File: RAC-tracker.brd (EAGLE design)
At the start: 31.8 x 97.8 mm, 37 parts, among them J1 U.FL, J2 U.FL, J5 U.FL, J6 U.FL, U2 SIM-ST-MFF2, U3 MCP73831, U4 NRF9160-SICA-R

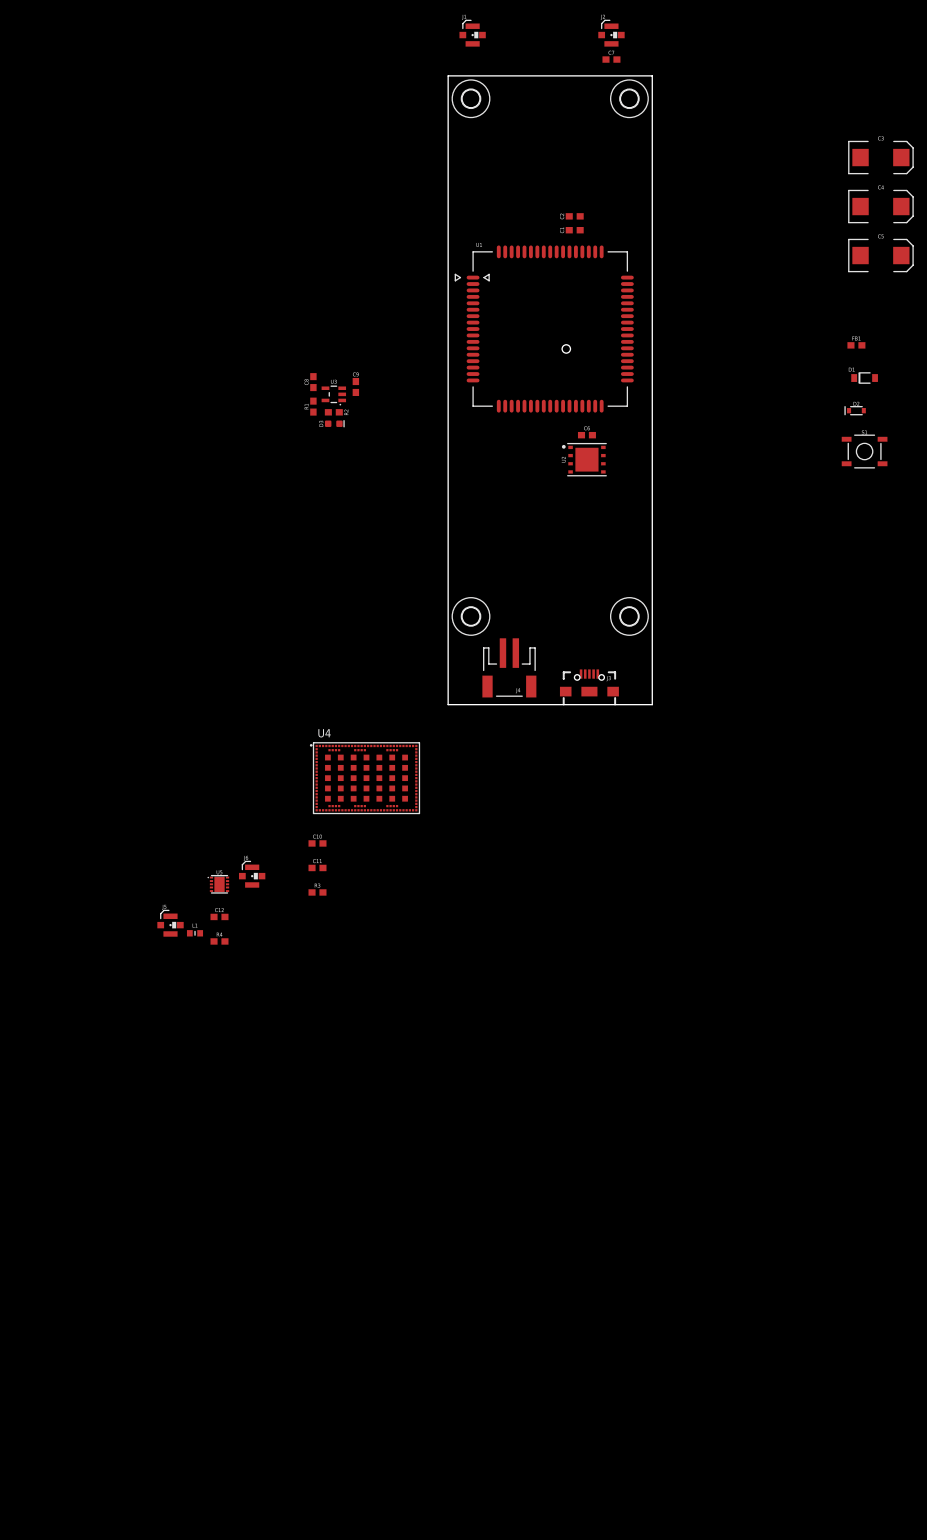
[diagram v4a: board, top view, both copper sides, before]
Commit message: Replaced GPS front-end, added 1.8V LDO
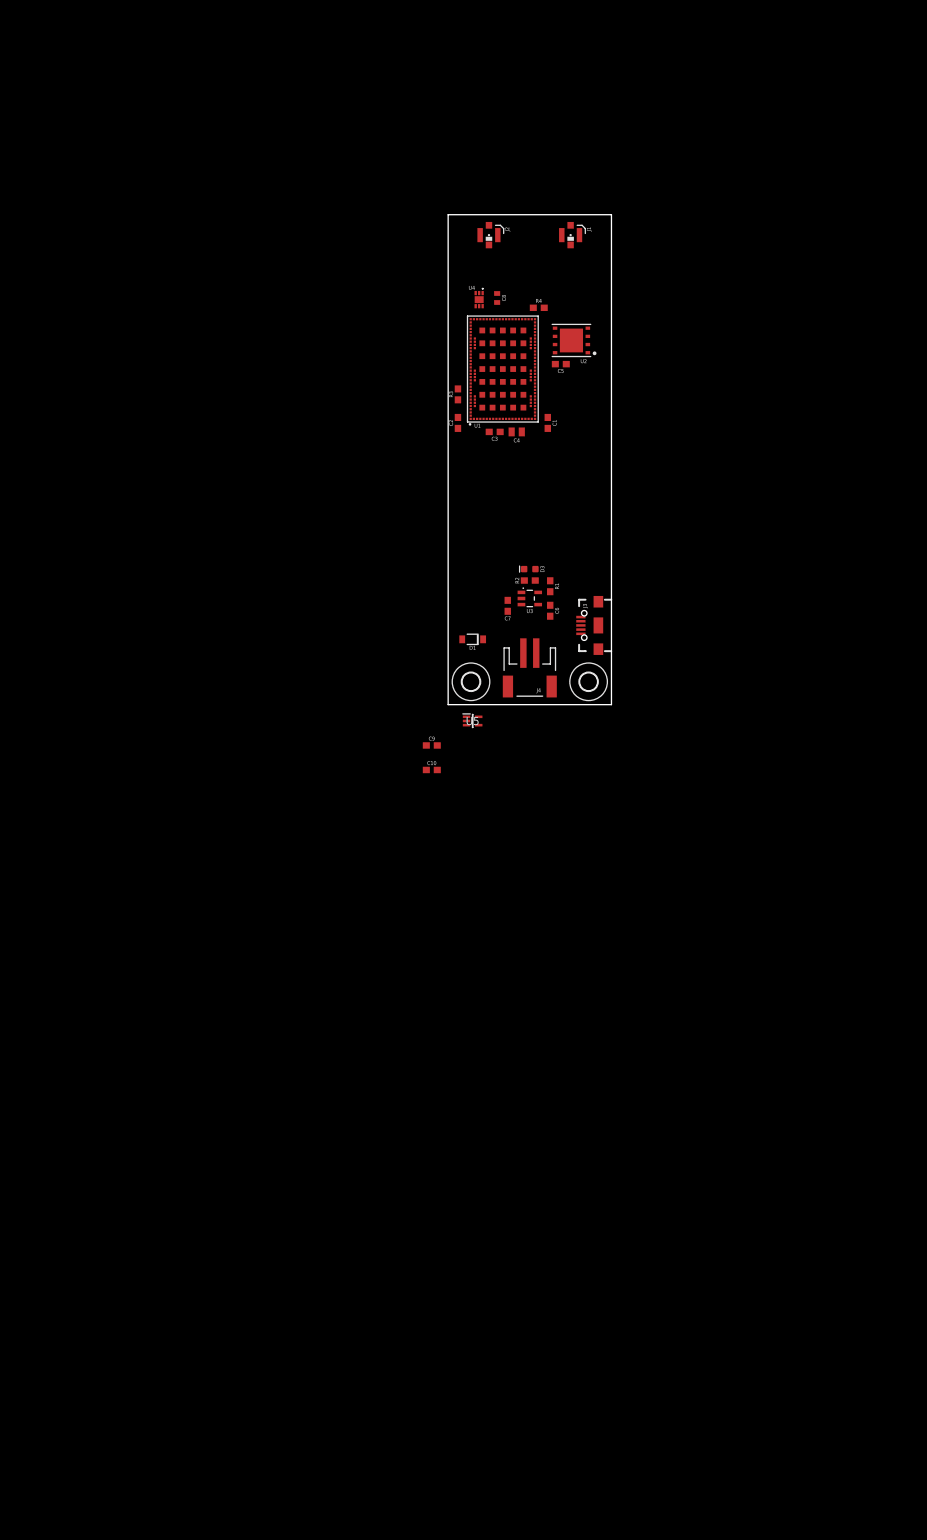
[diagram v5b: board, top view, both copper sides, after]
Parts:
- removed C11: 4.7uF, SparkFun-Capacitors:0603
- removed C12: 1nF, SparkFun-Capacitors:0603
- removed D2: 250mA/100V, SparkFun-DiscreteSemi:SOD-323
- removed FB1: 30Ω/1.8A, SparkFun-Coils:0603
- removed H3, H4: MOUNT-HOLE2.8, holes:2,8
- removed J5, J6: U.FL, SparkFun-Connectors:U.FL
- removed L1: 10nH, rocket-components:INDC1608X100N
- removed S1: MOMENTARY-SWITCH-SPST-SMD-5.2MM, SparkFun-Switches:TACTILE_SWITCH_SMD_5.2MM
- C1, C6: value 0.1uF -> 4.7uF
- C10, C9: value 4.7uF -> 1.0uF
- C2: value 1.0uF -> 4.7uF
- C3: value 100uF -> 4.7uF; device SparkFun-Capacitors:EIA7343 -> SparkFun-Capacitors:0603
- C4: value 100uF -> 47uF; device SparkFun-Capacitors:EIA7343 -> rocket-components:CAPC2012X145N
- C5: value 100uF -> 0.1uF; device SparkFun-Capacitors:EIA7343 -> SparkFun-Capacitors:0603
- C7: value 33pF -> 4.7uF
- C8: value 4.7uF -> 56pF; device SparkFun-Capacitors:0603 -> rocket-components:CAPC1608X90N
- U1: value (none) -> NRF9160-SICA-R; device rocket-components:SIM7000 -> rocket-components:NORDIC_NRF9160-SICA-R
- U4: value NRF9160-SICA-R -> SKY65723-81; device rocket-components:NORDIC_NRF9160-SICA-R -> rocket-components:SKY6572381
- U5: value (none) -> MIC5365-1.8YC5-TR; device rocket-components:HFFP10-CD -> rocket-components:SOT65P210X110-5N
- moved R4 110.4 mm to (14.1, 61.7), turned to 180 degrees
- moved H2 90.9 mm to (21.8, 3.56)
- moved H1 90.7 mm to (3.56, 3.56)
- moved C7 86.5 mm to (9.27, 15.4), turned to 90 degrees
- moved R3 80.5 mm to (1.52, 48.3), turned to 90 degrees
- moved U4 76.5 mm to (4.83, 63.0), turned to 180 degrees
- moved C3 73.7 mm to (7.24, 42.4), turned to 180 degrees
- moved D1 73.3 mm to (3.81, 10.2), turned to 180 degrees
- moved C4 66.6 mm to (10.7, 42.4)
- moved C9 57.0 mm to (-2.54, -6.35), turned to 0 degrees
- moved C5 52.6 mm to (17.5, 53.0)
- moved U5 46.9 mm to (3.81, -2.54)
- moved R1 46.2 mm to (15.9, 18.4), turned to 270 degrees
- moved U3 44.0 mm to (12.7, 16.5), turned to 270 degrees
- moved R2 40.2 mm to (12.7, 19.3), turned to 0 degrees
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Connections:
- removed net 3.3V: C11.1, C12.1, U4.12, U5.3
- removed net GNSS_OUT: C7.2, J2.FEED
- removed net GNSS_RF: C7.1, U1.53
- removed net IO_SUPPLY: U4.13
- removed net LTE_OUT: J1.FEED, U1.60
- removed net N$1: R3.1, U4.101
- removed net N$2: J6.FEED, U4.61
- removed net N$3: L1.2, U5.7
- removed net N$4: L1.1, U5.8
- removed net PWRKEY: D2.C, S1.3
- removed net PWRKEY_AN: D2.A, U1.1
- removed net RI: U1.4
- removed net RXD: U1.10
- removed net TXD: U1.9
- removed net VIN: C1.1, C2.1, C3.A, C4.A, C5.A, FB1.2, U1.55, U1.56, U1.57
- new net 1.8V: C10.1, C3.1, C8.1, U1.12, U4.1, U5.5
- new net EN: R3.1, U1.101
- new net IO_SUP: C4.1, U1.13
- new net LTE_ANT: J1.FEED, U1.61
- net GND: now also C3.2, C4.2, C5.2, C7.2, U1.1, U1.103_1, U1.103_10, U1.103_11, U1.103_12, U1.103_13, U1.103_14, U1.103_15, U1.103_16, U1.103_17, U1.103_18, U1.103_19, U1.103_2, U1.103_20, U1.103_21, U1.103_22, U1.103_23, U1.103_24, U1.103_25, U1.103_26, U1.103_27, U1.103_28, U1.103_29, U1.103_3, U1.103_30, U1.103_31, U1.103_32, U1.103_33, U1.103_34, U1.103_35, U1.103_4, U1.103_5, U1.103_6, U1.103_7, U1.103_8, U1.103_9, U1.14, U1.21, U1.27, U1.31, U1.36, U1.41, U1.44, U1.47, U1.5, U1.50, U1.52, U1.56, U1.60, U1.66, U1.72, U1.74, U1.75, U1.76, U1.77, U1.78, U1.79, U1.80, U1.81, U1.82, U1.85, U1.9, U1.90, U1.94, U1.98, U4.7; no longer C11.2, C12.2, C3.C, C4.C, C5.C, J5.1, J5.2, J6.1, J6.2, S1.1, U1.18, U1.2, U1.29, U1.39, U1.45, U1.46, U1.54, U1.58, U1.59, U1.61, U1.64, U4.1, U4.103_1, U4.103_10, U4.103_11, U4.103_12, U4.103_13, U4.103_14, U4.103_15, U4.103_16, U4.103_17, U4.103_18, U4.103_19, U4.103_2, U4.103_20, U4.103_21, U4.103_22, U4.103_23, U4.103_24, U4.103_25, U4.103_26, U4.103_27, U4.103_28, U4.103_29, U4.103_3, U4.103_30, U4.103_31, U4.103_32, U4.103_33, U4.103_34, U4.103_35, U4.103_4, U4.103_5, U4.103_6, U4.103_7, U4.103_8, U4.103_9, U4.14, U4.17, U4.21, U4.27, U4.31, U4.36, U4.41, U4.44, U4.47, U4.5, U4.50, U4.52, U4.56, U4.60, U4.62, U4.63, U4.65, U4.66, U4.72, U4.74, U4.75, U4.76, U4.77, U4.78, U4.79, U4.80, U4.81, U4.82, U4.85, U4.9, U4.90, U4.94, U4.98, U5.1, U5.4, U5.6, U5.9, U5.EP
- net GPS_ANT: now also J2.FEED, U4.3; no longer J5.FEED, U5.5
- net GPS_EN: now also U1.55, U4.2; no longer U4.55, U5.2
- net GPS_RF: now also U1.67, U4.6; no longer U4.67, U5.10
- net SIM_CLK: now also U1.46; no longer U1.32, U4.46
- net SIM_DATA: now also U1.48; no longer U1.31, U4.48
- net SIM_RST: now also U1.43; no longer U1.33, U4.43
- net SIM_VIN: now also C5.1, U1.49; no longer C6.1, U1.30, U4.49
- net USB_DM: no longer U1.28
- net USB_DP: no longer U1.27
- net VIO: now also U1.57; no longer U4.57
- net V_BATT: now also C1.1, C2.1, C7.1, U1.102, U1.22, U5.1; no longer C10.1, FB1.1, U4.102, U4.22
- net V_USB: now also C6.1; no longer C8.1, U1.24
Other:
- board size 31.8 x 97.8 mm -> 25.4 x 76.2 mm

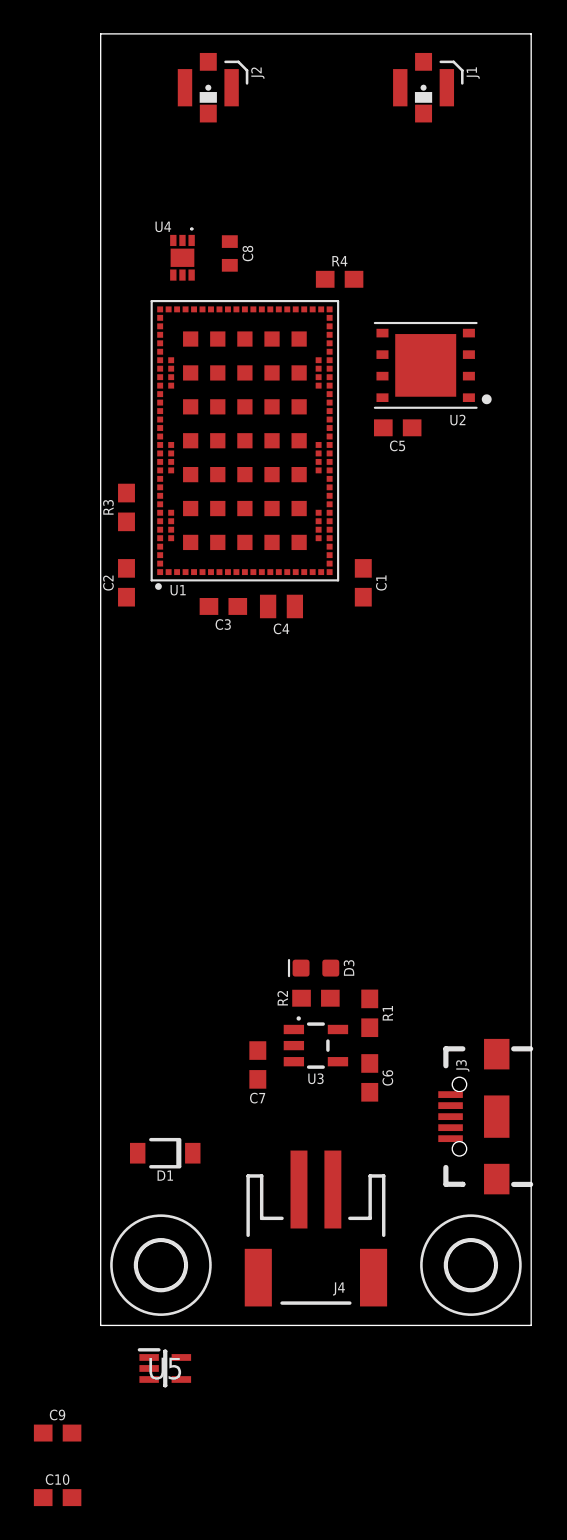
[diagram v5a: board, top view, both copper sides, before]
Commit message: Fixed missing LDO nets, started routing board
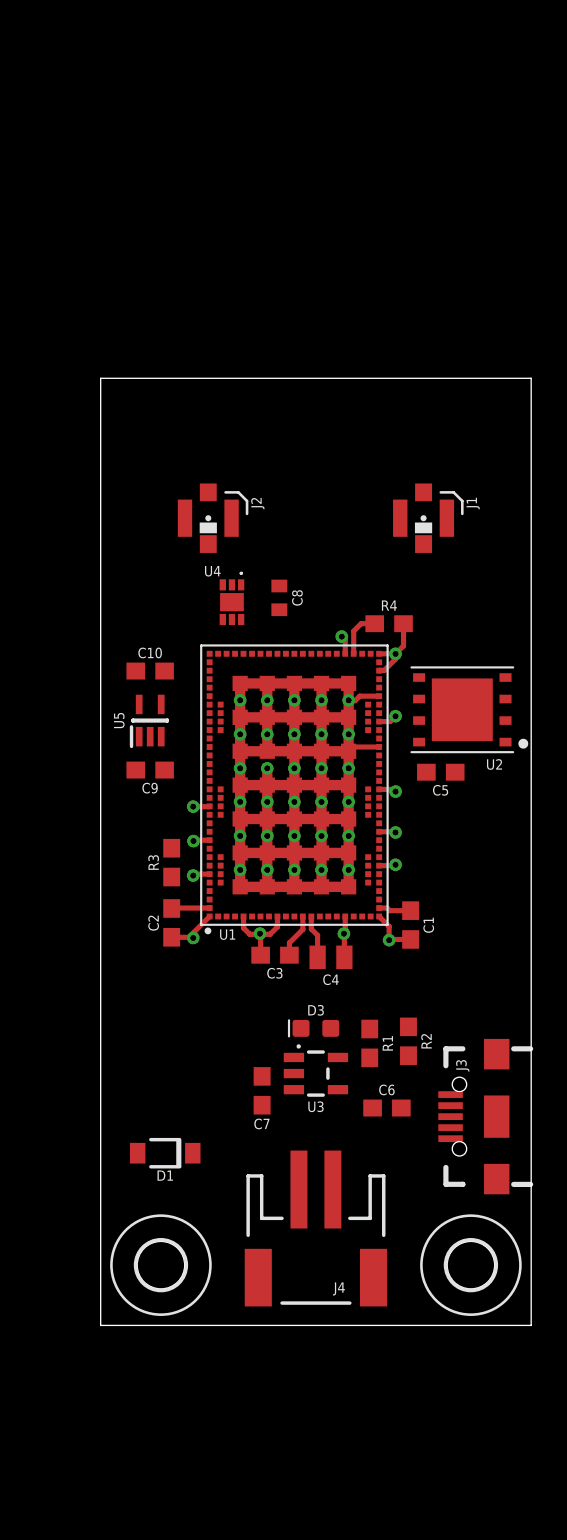
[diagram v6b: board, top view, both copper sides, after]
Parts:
- moved C10 49.1 mm to (2.92, 38.6)
- moved C9 39.5 mm to (2.92, 32.8)
- moved U5 38.2 mm to (2.92, 35.7), turned to 90 degrees
- moved J1 25.4 mm to (19.1, 47.6)
- moved J2 25.4 mm to (6.35, 47.6)
- moved R3 21.1 mm to (4.19, 27.3)
- moved C4 20.9 mm to (13.6, 21.7)
- moved C3 20.8 mm to (10.3, 21.8)
- moved U1 20.5 mm to (11.4, 31.9)
- moved C8 20.5 mm to (10.5, 42.9)
- moved R4 20.5 mm to (17.0, 41.4)
- moved U4 20.5 mm to (7.75, 42.7)
- moved C5 20.5 mm to (20.1, 32.6)
- moved U2 20.4 mm to (21.3, 36.3)
- moved C1 20.4 mm to (18.3, 23.6)
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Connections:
- net GND: now also U5.2
- net V_BATT: now also U5.3
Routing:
- net GND: track 0.00 -> 133.5 mm, vias 0 -> 43
- net V_BATT: track 0.00 -> 4.17 mm
- net GPS_EN: track 0.00 -> 2.76 mm
- net 1.8V: track 0.00 -> 2.61 mm
- net IO_SUP: track 0.00 -> 2.56 mm
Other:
- board size 25.4 x 76.2 mm -> 25.4 x 55.9 mm

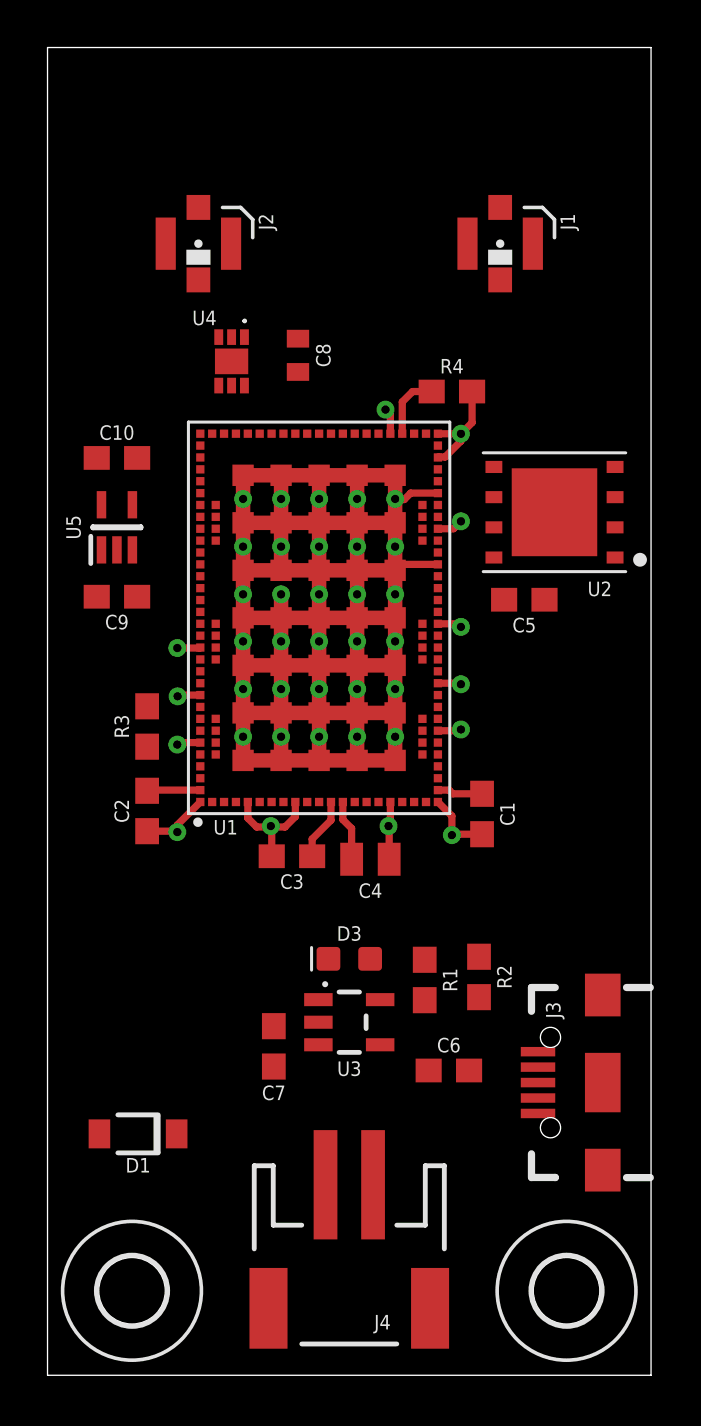
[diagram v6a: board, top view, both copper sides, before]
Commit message: Completed routing, cleared DRC errors
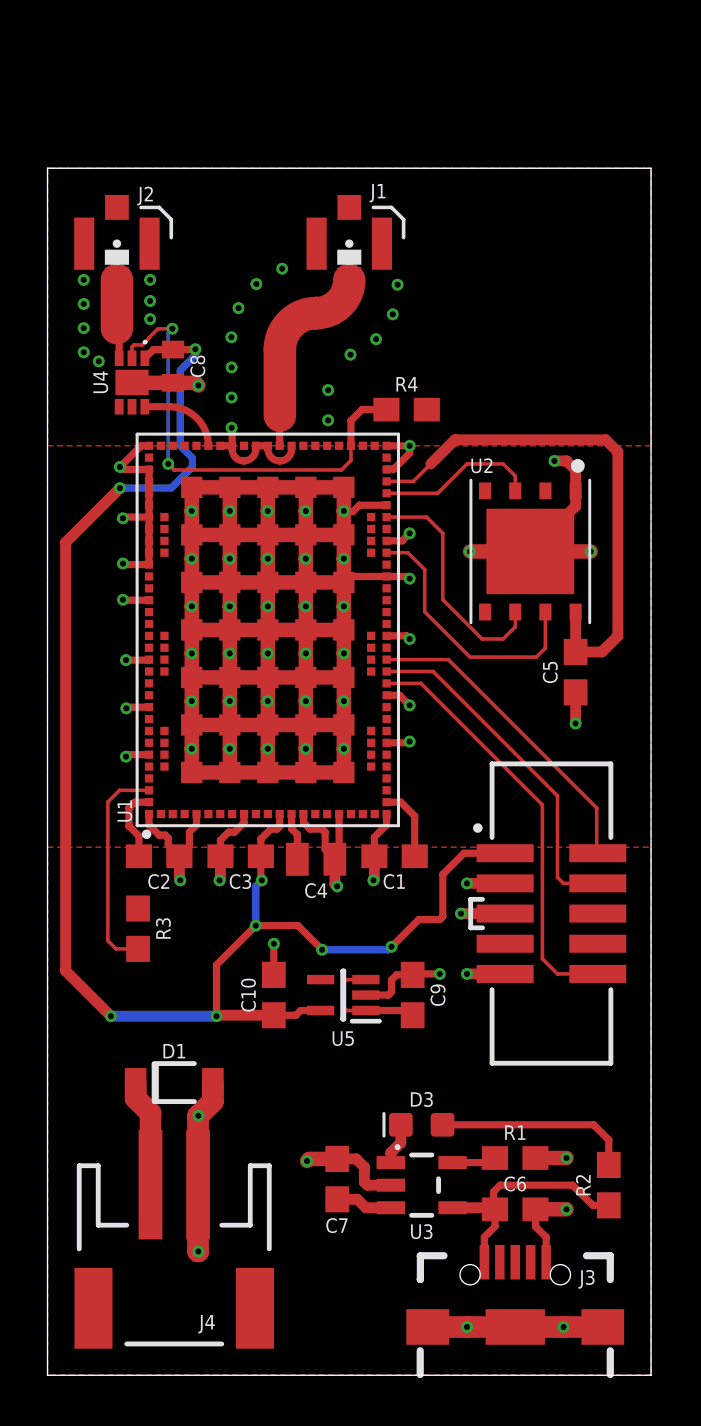
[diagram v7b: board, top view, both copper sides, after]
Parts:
- removed H1, H2: MOUNT-HOLE2.8, holes:2,8
- added J5: CORTEX_JTAG_DEBUG_MINIMUM_SMD, SparkFun-Connectors:2X5-SMD-1.27MM
- moved C10 23.6 mm to (9.53, 16.0), turned to 90 degrees
- moved U5 21.9 mm to (12.4, 16.0), turned to 180 degrees
- moved C9 20.9 mm to (15.4, 16.0), turned to 90 degrees
- moved J3 10.9 mm to (19.7, 2.03), turned to 90 degrees
- moved R2 10.3 mm to (23.6, 8.00)
- moved R3 8.52 mm to (3.81, 18.8)
- moved R1 8.41 mm to (19.7, 9.14), turned to 180 degrees
- moved D3 7.62 mm to (15.7, 10.5)
- moved U3 7.50 mm to (15.7, 8.00)
- moved J4 7.37 mm to (5.33, 4.32)
- moved C6 6.48 mm to (19.7, 6.99)
- moved J1 6.35 mm to (12.7, 47.6)
- moved C7 6.19 mm to (12.2, 8.26)
- moved C8 5.28 mm to (5.28, 42.5)
- moved U4 4.28 mm to (3.56, 41.8)
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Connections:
- new net !RST: J5.10, U1.32
- new net SWDCLK: J5.4, U1.33
- new net SWDIO: J5.2, U1.34
- net 1.8V: now also J5.1
- net GND: now also J5.3, J5.5, J5.9
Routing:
- net GND: track 133.5 -> 201.4 mm, vias 43 -> 85
- net 1.8V: track 2.61 -> 67.5 mm, vias 0 -> 8
- net SIM_VIN: track 0.00 -> 22.2 mm
- net !RST: track 0.00 -> 17.7 mm
- net GPS_EN: track 2.76 -> 19.6 mm, vias 0 -> 2
- net SWDCLK: track 0.00 -> 14.6 mm
- net V_BATT: track 4.17 -> 18.3 mm
- net SWDIO: track 0.00 -> 13.4 mm
- net SIM_RST: track 0.00 -> 11.2 mm
- net V_USB: track 0.00 -> 10.2 mm
- net SIM_CLK: track 0.00 -> 10.0 mm
- net EN: track 0.00 -> 9.19 mm
- net STAT_AN: track 0.00 -> 8.32 mm
- net LTE_ANT: track 0.00 -> 8.19 mm
- net SIM_DATA: track 0.00 -> 6.76 mm
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- added copper zone on layer 1, net GND
- added copper zone on layer 16, net GND
- added copper zone on layer 1, net V_BATT
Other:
- board size 25.4 x 55.9 mm -> 25.4 x 50.8 mm
